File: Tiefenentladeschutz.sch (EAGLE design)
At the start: 25 parts, among them IC1 ICL7665CSA, Q4 NMOSFET-D2PAK-7

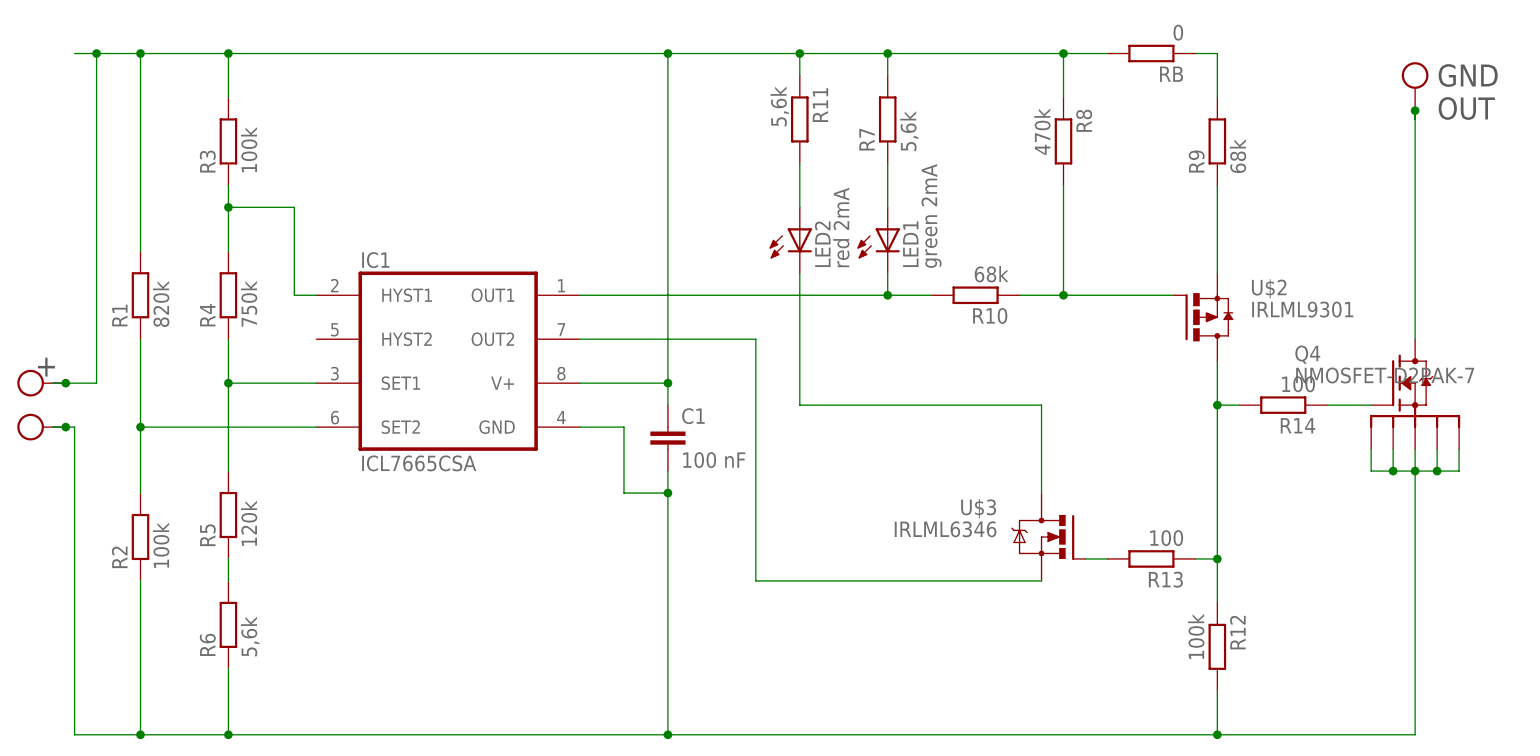
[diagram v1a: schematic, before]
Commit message: Ohne LED added, replaced P-mosfet by bipolar
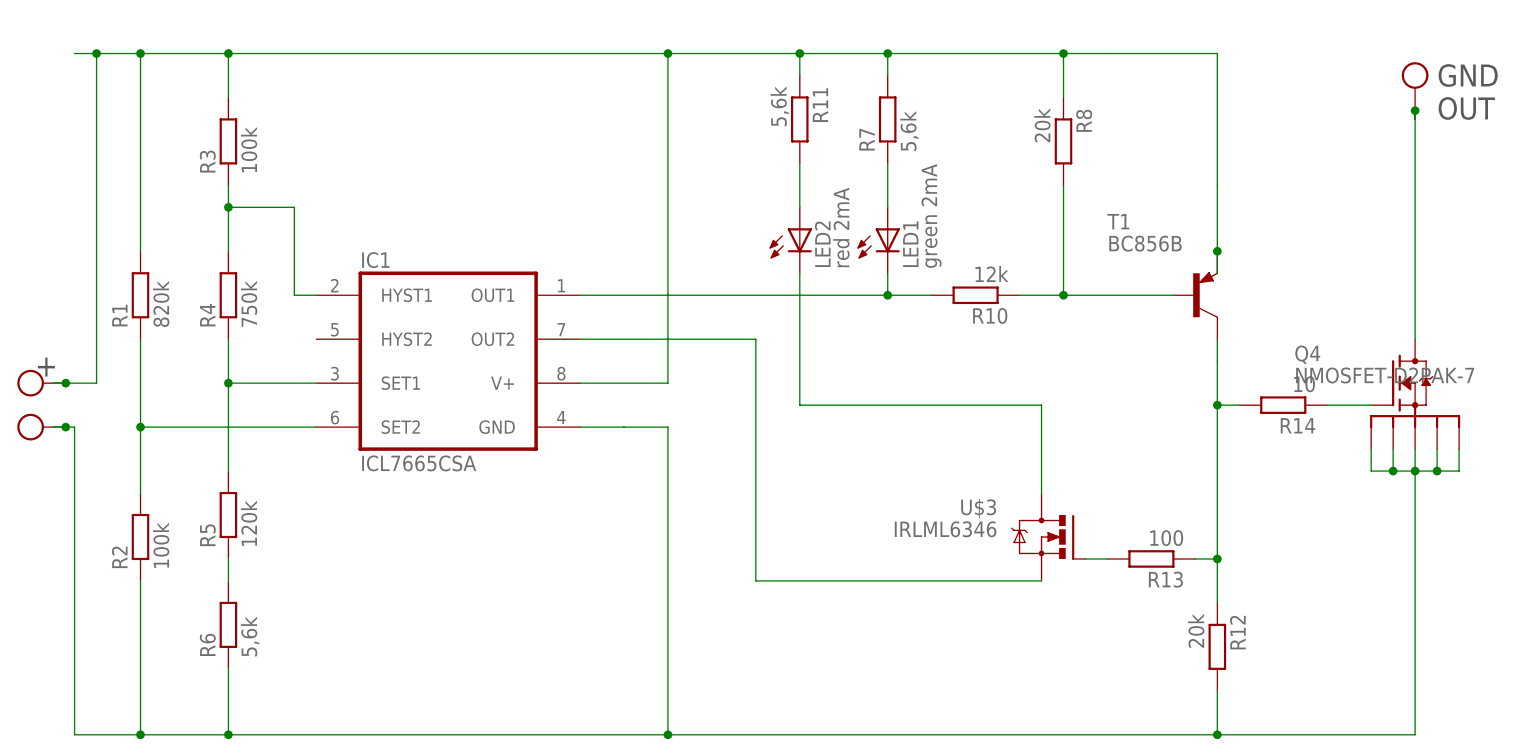
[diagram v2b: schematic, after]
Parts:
- removed C1: 100 nF, eagle-ltspice:CC1206
- removed R9: 68k, eagle-ltspice:RR1206
- removed RB: 0, eagle-ltspice:RR1206
- removed U$2: IRLML9301, 0liver:IRLML9301
- added T1: BC856B, transistor:BC856B-PNP-SOT23-BEC
- R10: value 68k -> 12k
- R12: value 100k -> 20k
- R13: device eagle-ltspice:RR1206 -> rcl:R-EU_R1206
- R14: value 100 -> 10; device eagle-ltspice:RR1206 -> rcl:R-EU_R0603
- R3, R4, R7: device eagle-ltspice:RR1206 -> rcl:R-EU_R0603
- R8: value 470k -> 20k; device eagle-ltspice:RR1206 -> rcl:R-EU_R0603
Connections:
- removed net N$10: R9.2, RB.1
- removed net N$8: R9.1, U$2.S
- net GND: no longer C1.2
- net N$22: now also T1.C; no longer U$2.D
- net N$7: now also T1.B; no longer U$2.G
- net V+: now also T1.E; no longer C1.1, RB.2
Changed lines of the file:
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@@
 <?xml version="1.0" encoding="utf-8"?>
 <!DOCTYPE eagle SYSTEM "eagle.dtd">
-<eagle version="7.5.0">
+<eagle version="8.0.1">
 <drawing>
 <settings>
@@
 </classes>
 <parts>
-<part name="R4" library="eagle-ltspice" deviceset="R" device="R1206" value="750k"/>
+<part name="R4" library="rcl" deviceset="R-EU_" device="R0603" value="750k"/>
 <part name="R5" library="eagle-ltspice" deviceset="R" device="R1206" value="120k"/>
 <part name="R1" library="eagle-ltspice" deviceset="R" device="R1206" value="820k"/>
 <part name="R2" library="eagle-ltspice" deviceset="R" device="R1206" value="100k"/>
 <part name="R11" library="eagle-ltspice" deviceset="R" device="R1206" value="5,6k"/>
-<part name="R8" library="eagle-ltspice" deviceset="R" device="R1206" value="470k"/>
+<part name="R8" library="rcl" deviceset="R-EU_" device="R0603" value="20k"/>
 <part name="IC1" library="maxim" deviceset="ICL7665CSA" device=""/>
-<part name="C1" library="eagle-ltspice" deviceset="C" device="C1206" value="100 nF"/>
 <part name="LED2" library="eagle-ltspice" deviceset="LED_E" device="SML0603" value="red 2mA"/>
 <part name="LED1" library="eagle-ltspice" deviceset="LED_E" device="SML0603" value="green 2mA"/>
-<part name="R7" library="eagle-ltspice" deviceset="R" device="R1206" value="5,6k"/>
-<part name="R10" library="eagle-ltspice" deviceset="R" device="R1206" value="68k"/>
+<part name="R7" library="rcl" deviceset="R-EU_" device="R0603" value="5,6k"/>
+<part name="R10" library="eagle-ltspice" deviceset="R" device="R1206" value="12k"/>
 <part name="R6" library="eagle-ltspice" deviceset="R" device="R1206" value="5,6k"/>
-<part name="R9" library="eagle-ltspice" deviceset="R" device="R1206" value="68k"/>
-<part name="R3" library="eagle-ltspice" deviceset="R" device="R1206" value="100k"/>
-<part name="R12" library="eagle-ltspice" deviceset="R" device="R1206" value="100k"/>
-<part name="U$2" library="0liver" deviceset="IRLML9301" device=""/>
+<part name="R3" library="rcl" deviceset="R-EU_" device="R0603" value="100k"/>
+<part name="R12" library="eagle-ltspice" deviceset="R" device="R1206" value="20k"/>
 <part name="U$3" library="0liver" deviceset="IRLML6346" device=""/>
 <part name="U$4" library="0liver" deviceset="PIN" device="BIG"/>
 <part name="U$6" library="0liver" deviceset="PIN" device="1.27"/>
 <part name="U$7" library="0liver" deviceset="PIN" device="1.27"/>
-<part name="RB" library="eagle-ltspice" deviceset="R" device="R1206" value="0"/>
 <part name="Q4" library="D2pak-7" deviceset="NMOSFET-D2PAK-7" device=""/>
-<part name="R13" library="eagle-ltspice" deviceset="R" device="R1206" value="100"/>
-<part name="R14" library="eagle-ltspice" deviceset="R" device="R1206" value="100"/>
+<part name="R13" library="rcl" deviceset="R-EU_" device="R1206" value="100"/>
+<part name="R14" library="rcl" deviceset="R-EU_" device="R0603" value="10"/>
+<part name="T1" library="transistor" deviceset="*-PNP-" device="SOT23-BEC" technology="BC856B" value="BC856B"/>
 </parts>
 <sheets>
@@
 <instance part="R8" gate="G$1" x="86.36" y="86.36" rot="R270"/>
 <instance part="IC1" gate="G$1" x="15.24" y="60.96"/>
-<instance part="C1" gate="G$1" x="40.64" y="53.34"/>
 <instance part="LED2" gate="G$1" x="55.88" y="76.2"/>
 <instance part="LED1" gate="G$1" x="66.04" y="76.2"/>
@@
 <instance part="R10" gate="G$1" x="76.2" y="68.58" rot="R180"/>
 <instance part="R6" gate="G$1" x="-10.16" y="30.48" rot="R90"/>
-<instance part="R9" gate="G$1" x="104.14" y="86.36" rot="R90"/>
 <instance part="R3" gate="G$1" x="-10.16" y="86.36" rot="R90"/>
 <instance part="R12" gate="G$1" x="104.14" y="27.94" rot="R270"/>
-<instance part="U$2" gate="G$1" x="101.6" y="66.04"/>
 <instance part="U$3" gate="G$1" x="86.36" y="40.64" rot="MR0"/>
 <instance part="U$4" gate="G$1" x="-33.02" y="58.42" rot="R90"/>
 <instance part="U$6" gate="G$1" x="-33.02" y="53.34" rot="R90"/>
 <instance part="U$7" gate="G$1" x="127" y="93.98"/>
-<instance part="RB" gate="G$1" x="96.52" y="96.52" rot="R180"/>
 <instance part="Q4" gate="G$1" x="124.46" y="58.42"/>
 <instance part="R13" gate="G$1" x="96.52" y="38.1" rot="R180"/>
 <instance part="R14" gate="G$1" x="111.76" y="55.88" rot="R180"/>
+<instance part="T1" gate="G$1" x="101.6" y="68.58"/>
 </instances>
 <busses>
@@
 <pinref part="IC1" gate="G$1" pin="GND"/>
 <wire x1="30.48" y1="53.34" x2="35.56" y2="53.34" width="0.1524" layer="91"/>
-<wire x1="35.56" y1="53.34" x2="35.56" y2="45.72" width="0.1524" layer="91"/>
-<wire x1="35.56" y1="45.72" x2="40.64" y2="45.72" width="0.1524" layer="91"/>
-<wire x1="40.64" y1="45.72" x2="40.64" y2="17.78" width="0.1524" layer="91"/>
-<pinref part="C1" gate="G$1" pin="2"/>
-<wire x1="40.64" y1="45.72" x2="40.64" y2="48.26" width="0.1524" layer="91"/>
-<junction x="40.64" y="45.72"/>
+<wire x1="35.56" y1="53.34" x2="40.64" y2="53.34" width="0.1524" layer="91"/>
+<wire x1="40.64" y1="53.34" x2="40.64" y2="17.78" width="0.1524" layer="91"/>
 <pinref part="R2" gate="G$1" pin="1"/>
 <wire x1="-20.32" y1="35.56" x2="-20.32" y2="17.78" width="0.1524" layer="91"/>
@@
 <wire x1="99.06" y1="68.58" x2="86.36" y2="68.58" width="0.1524" layer="91"/>
 <wire x1="81.28" y1="68.58" x2="86.36" y2="68.58" width="0.1524" layer="91"/>
-<pinref part="U$2" gate="G$1" pin="G"/>
+<pinref part="T1" gate="G$1" pin="B"/>
 </segment>
 </net>
@@
 <junction x="104.14" y="38.1"/>
 <wire x1="104.14" y1="60.96" x2="104.14" y2="55.88" width="0.1524" layer="91"/>
-<pinref part="U$2" gate="G$1" pin="D"/>
 <wire x1="104.14" y1="55.88" x2="106.68" y2="55.88" width="0.1524" layer="91"/>
 <pinref part="R13" gate="G$1" pin="1"/>
 <pinref part="R14" gate="G$1" pin="2"/>
+<pinref part="T1" gate="G$1" pin="C"/>
+<wire x1="104.14" y1="63.5" x2="104.14" y2="60.96" width="0.1524" layer="91"/>
 </segment>
 </net>
@@
 <wire x1="30.48" y1="58.42" x2="40.64" y2="58.42" width="0.1524" layer="91"/>
 <wire x1="40.64" y1="58.42" x2="40.64" y2="96.52" width="0.1524" layer="91"/>
-<pinref part="C1" gate="G$1" pin="1"/>
-<wire x1="40.64" y1="58.42" x2="40.64" y2="55.88" width="0.1524" layer="91"/>
-<junction x="40.64" y="58.42"/>
 <junction x="40.64" y="96.52"/>
 <pinref part="R8" gate="G$1" pin="1"/>
@@
 <wire x1="-25.4" y1="58.42" x2="-25.4" y2="96.52" width="0.1524" layer="91"/>
 <junction x="-25.4" y="96.52"/>
-<pinref part="RB" gate="G$1" pin="2"/>
 <wire x1="86.36" y1="96.52" x2="91.44" y2="96.52" width="0.1524" layer="91"/>
 <junction x="86.36" y="96.52"/>
+<wire x1="104.14" y1="81.28" x2="104.14" y2="73.66" width="0.1524" layer="91"/>
+<pinref part="T1" gate="G$1" pin="E"/>
+<wire x1="104.14" y1="73.66" x2="104.14" y2="71.12" width="0.1524" layer="91"/>
+<junction x="104.14" y="73.66"/>
+<wire x1="91.44" y1="96.52" x2="104.14" y2="96.52" width="0.1524" layer="91"/>
+<wire x1="104.14" y1="96.52" x2="104.14" y2="81.28" width="0.1524" layer="91"/>
 </segment>
 </net>
@@
 </segment>
 </net>
-<net name="N$8" class="0">
-<segment>
-<pinref part="R9" gate="G$1" pin="1"/>
-<wire x1="104.14" y1="81.28" x2="104.14" y2="71.12" width="0.1524" layer="91"/>
-<pinref part="U$2" gate="G$1" pin="S"/>
-</segment>
-</net>
-<net name="N$10" class="0">
-<segment>
-<wire x1="104.14" y1="91.44" x2="104.14" y2="96.52" width="0.1524" layer="91"/>
-<pinref part="R9" gate="G$1" pin="2"/>
-<pinref part="RB" gate="G$1" pin="1"/>
-<wire x1="101.6" y1="96.52" x2="104.14" y2="96.52" width="0.1524" layer="91"/>
-</segment>
-</net>

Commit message: R12 to 100 kOhm
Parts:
- R12: value 20k -> 100k
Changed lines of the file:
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@@
 <part name="R6" library="eagle-ltspice" deviceset="R" device="R1206" value="5,6k"/>
 <part name="R3" library="rcl" deviceset="R-EU_" device="R0603" value="100k"/>
-<part name="R12" library="eagle-ltspice" deviceset="R" device="R1206" value="20k"/>
+<part name="R12" library="eagle-ltspice" deviceset="R" device="R1206" value="100k"/>
 <part name="U$3" library="0liver" deviceset="IRLML6346" device=""/>
 <part name="U$4" library="0liver" deviceset="PIN" device="BIG"/>
